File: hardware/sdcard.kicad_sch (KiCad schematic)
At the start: 15 parts, among them J4 MEM2067

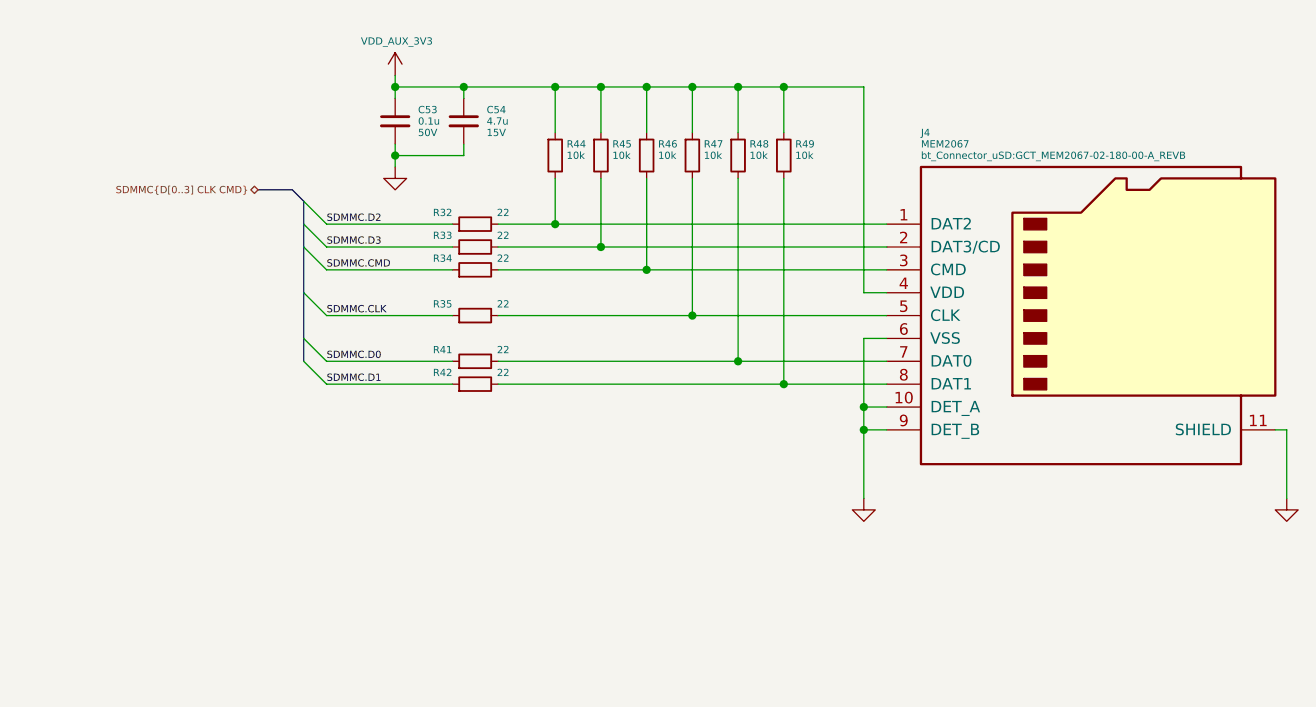
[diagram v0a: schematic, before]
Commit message: minor sch tweaks, more layout, added power emc shield
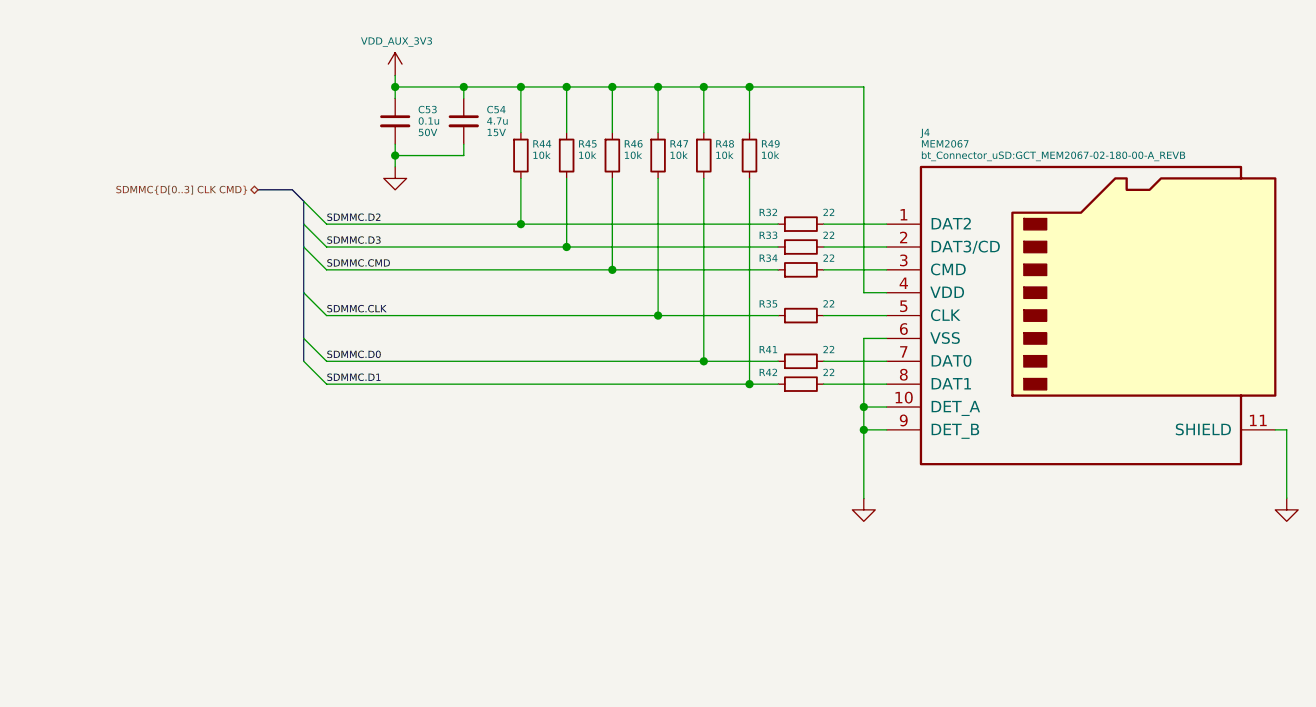
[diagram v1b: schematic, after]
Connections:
- net SDMMC.CLK: now also R47.2
- net SDMMC.CMD: now also R46.2
- net SDMMC.D0: now also R48.2
- net SDMMC.D1: now also R49.2
- net SDMMC.D2: now also R44.2
- net SDMMC.D3: now also R45.2
- net at J4.1 (DAT2), R32.2: no longer R44.2
- net at J4.8 (DAT1), R42.2: no longer R49.2
- net at J4.2 (DAT3/CD), R33.2: no longer R45.2
- net at J4.7 (DAT0), R41.2: no longer R48.2
- net at J4.3 (CMD), R34.2: no longer R46.2
- net at J4.5 (CLK), R35.2: no longer R47.2
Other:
- moved on the sheet: R32, R33, R34, R35, R41, R42, R44, R45, R46, R47, R48, R49

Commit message: Added ESP32-S3-WROOM
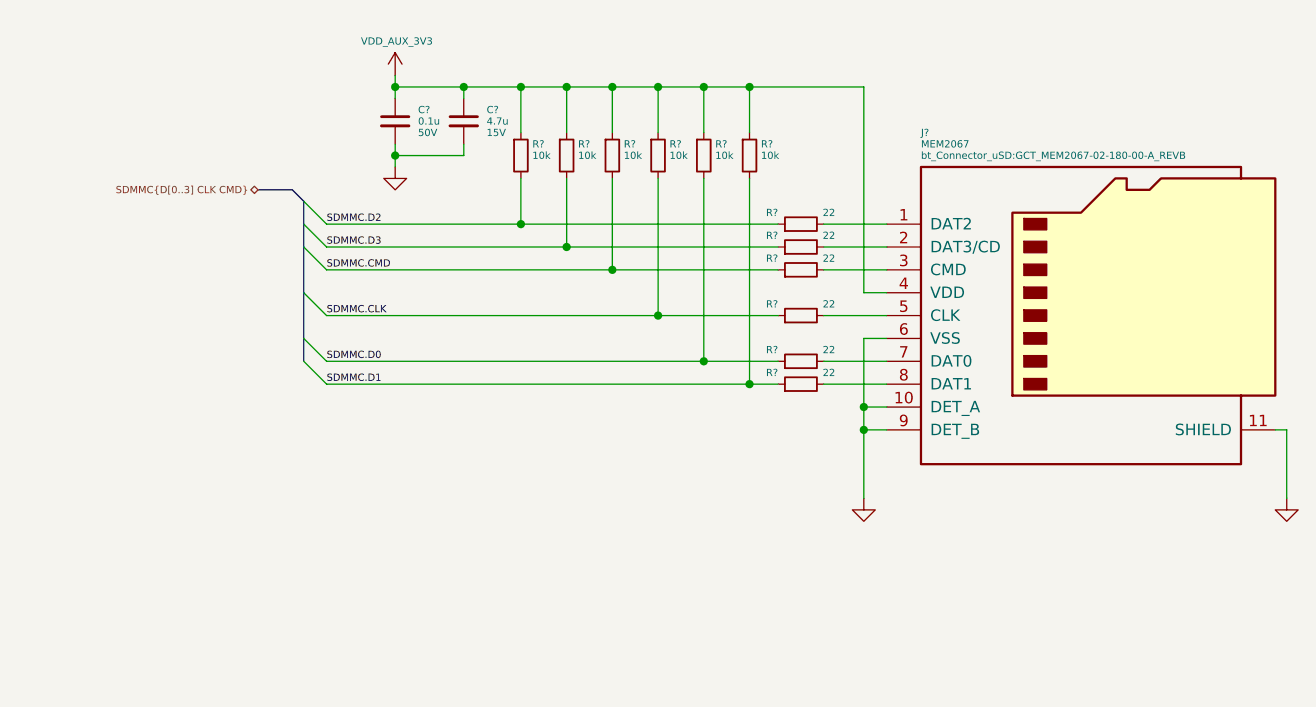
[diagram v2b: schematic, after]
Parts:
- renumbered C54 to C?, C53 to C?, J4 to J?, R44 to R?, R42 to R?, R33 to R?, R49 to R?, R41 to R?, R46 to R?, R45 to R?, R35 to R?, R48 to R?, R32 to R?, R34 to R?, R47 to R?
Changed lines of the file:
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@@
   (symbol (lib_id "Device:R_Small") (at 118.11 82.55 0) (unit 1)
     (in_bom yes) (on_board yes)
-    (property "Reference" "R44" (id 0) (at 119.38 81.28 0)
+    (property "Reference" "R?" (id 0) (at 119.38 81.28 0)
       (effects (font (size 0.8 0.8)) (justify left))
     )
@@
   (symbol (lib_id "Device:R_Small") (at 149.225 107.95 90) (unit 1)
     (in_bom yes) (on_board yes)
-    (property "Reference" "R42" (id 0) (at 146.685 106.68 90)
+    (property "Reference" "R?" (id 0) (at 146.685 106.68 90)
       (effects (font (size 0.8 0.8)) (justify left))
     )
@@
   (symbol (lib_id "Device:C_Small") (at 111.76 78.74 0) (unit 1)
     (in_bom yes) (on_board yes)
-    (property "Reference" "C54" (id 0) (at 114.3 77.47 0)
+    (property "Reference" "C?" (id 0) (at 114.3 77.47 0)
       (effects (font (size 0.8 0.8)) (justify left))
     )
@@
   (symbol (lib_id "bt_power:VDD_AUX_3V3") (at 104.14 73.66 0) (unit 1)
     (in_bom no) (on_board no)
-    (property "Reference" "#U025" (id 0) (at 104.6734 73.66 0)
+    (property "Reference" "#U?" (id 0) (at 104.6734 73.66 0)
       (effects (font (size 1.27 1.27)) hide)
     )
@@
   (symbol (lib_id "Device:R_Small") (at 149.225 92.71 90) (unit 1)
     (in_bom yes) (on_board yes)
-    (property "Reference" "R33" (id 0) (at 146.685 91.44 90)
+    (property "Reference" "R?" (id 0) (at 146.685 91.44 90)
       (effects (font (size 0.8 0.8)) (justify left))
     )
@@
   (symbol (lib_id "Device:R_Small") (at 143.51 82.55 0) (unit 1)
     (in_bom yes) (on_board yes)
-    (property "Reference" "R49" (id 0) (at 144.78 81.28 0)
+    (property "Reference" "R?" (id 0) (at 144.78 81.28 0)
       (effects (font (size 0.8 0.8)) (justify left))
     )
@@
   (symbol (lib_id "Device:R_Small") (at 149.225 105.41 90) (unit 1)
     (in_bom yes) (on_board yes)
-    (property "Reference" "R41" (id 0) (at 146.685 104.14 90)
+    (property "Reference" "R?" (id 0) (at 146.685 104.14 90)
       (effects (font (size 0.8 0.8)) (justify left))
     )
@@
   (symbol (lib_id "power:GND") (at 156.21 120.65 0) (unit 1)
     (in_bom yes) (on_board yes)
-    (property "Reference" "#PWR072" (id 0) (at 156.21 127 0)
+    (property "Reference" "#PWR?" (id 0) (at 156.21 127 0)
       (effects (font (size 0.8 0.8)) hide)
     )
@@
   (symbol (lib_id "Device:R_Small") (at 128.27 82.55 0) (unit 1)
     (in_bom yes) (on_board yes)
-    (property "Reference" "R46" (id 0) (at 129.54 81.28 0)
+    (property "Reference" "R?" (id 0) (at 129.54 81.28 0)
       (effects (font (size 0.8 0.8)) (justify left))
     )
@@
   (symbol (lib_id "Device:R_Small") (at 123.19 82.55 0) (unit 1)
     (in_bom yes) (on_board yes)
-    (property "Reference" "R45" (id 0) (at 124.46 81.28 0)
+    (property "Reference" "R?" (id 0) (at 124.46 81.28 0)
       (effects (font (size 0.8 0.8)) (justify left))
     )
@@
   (symbol (lib_id "power:GND") (at 104.14 83.82 0) (mirror y) (unit 1)
     (in_bom yes) (on_board yes)
-    (property "Reference" "#PWR071" (id 0) (at 104.14 90.17 0)
+    (property "Reference" "#PWR?" (id 0) (at 104.14 90.17 0)
       (effects (font (size 0.8 0.8)) hide)
     )
@@
   (symbol (lib_id "Device:R_Small") (at 149.225 100.33 90) (unit 1)
     (in_bom yes) (on_board yes)
-    (property "Reference" "R35" (id 0) (at 146.685 99.06 90)
+    (property "Reference" "R?" (id 0) (at 146.685 99.06 90)
       (effects (font (size 0.8 0.8)) (justify left))
     )
@@
   (symbol (lib_id "Device:R_Small") (at 138.43 82.55 0) (unit 1)
     (in_bom yes) (on_board yes)
-    (property "Reference" "R48" (id 0) (at 139.7 81.28 0)
+    (property "Reference" "R?" (id 0) (at 139.7 81.28 0)
       (effects (font (size 0.8 0.8)) (justify left))
     )
@@
   (symbol (lib_id "power:GND") (at 203.2 120.65 0) (unit 1)
     (in_bom yes) (on_board yes)
-    (property "Reference" "#PWR073" (id 0) (at 203.2 127 0)
+    (property "Reference" "#PWR?" (id 0) (at 203.2 127 0)
       (effects (font (size 0.8 0.8)) hide)
     )
@@
   (symbol (lib_id "Device:C_Small") (at 104.14 78.74 0) (unit 1)
     (in_bom yes) (on_board yes)
-    (property "Reference" "C53" (id 0) (at 106.68 77.47 0)
+    (property "Reference" "C?" (id 0) (at 106.68 77.47 0)
       (effects (font (size 0.8 0.8)) (justify left))
     )
@@
   (symbol (lib_id "Connector:Micro_SD_Card_Det") (at 181.61 100.33 0) (unit 1)
     (in_bom yes) (on_board yes)
-    (property "Reference" "J4" (id 0) (at 162.56 80.01 0)
+    (property "Reference" "J?" (id 0) (at 162.56 80.01 0)
       (effects (font (size 0.8 0.8)) (justify left))
     )
@@
   (symbol (lib_id "Device:R_Small") (at 149.225 90.17 90) (unit 1)
     (in_bom yes) (on_board yes)
-    (property "Reference" "R32" (id 0) (at 146.685 88.9 90)
+    (property "Reference" "R?" (id 0) (at 146.685 88.9 90)
       (effects (font (size 0.8 0.8)) (justify left))
     )
@@
   (symbol (lib_id "Device:R_Small") (at 149.225 95.25 90) (unit 1)
     (in_bom yes) (on_board yes)
-    (property "Reference" "R34" (id 0) (at 146.685 93.98 90)
+    (property "Reference" "R?" (id 0) (at 146.685 93.98 90)
       (effects (font (size 0.8 0.8)) (justify left))
     )
@@
   (symbol (lib_id "Device:R_Small") (at 133.35 82.55 0) (unit 1)
     (in_bom yes) (on_board yes)
-    (property "Reference" "R47" (id 0) (at 134.62 81.28 0)
-      (effects (font (size 0.8 0.8)) (justify left))
-    )
+    (property "Reference" "R?" (id 0) (at 134.62 81.28 0)
+      (effects (font (size 0.8 0.8)) (justify left))
+    )

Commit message: changing sdmmc to spi to support lcd rgb mode
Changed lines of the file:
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@@
   (junction (at 128.27 74.93) (diameter 0) (color 0 0 0 0)
   )
+  (bus_entry (at 90.17 135.89) (size 2.54 -2.54)
+    (stroke (width 0) (type default) (color 0 0 0 0))
+  )
+  (bus_entry (at 92.71 125.73) (size -2.54 2.54)
+    (stroke (width 0) (type default) (color 0 0 0 0))
+  )
+  (bus_entry (at 92.71 130.81) (size -2.54 2.54)
+    (stroke (width 0) (type default) (color 0 0 0 0))
+  )
   (bus_entry (at 93.98 92.71) (size 2.54 2.54)
     (stroke (width 0) (type default) (color 0 0 0 0))
@@
     (stroke (width 0) (type default) (color 0 0 0 0))
   )
+  (bus_entry (at 92.71 133.35) (size -2.54 2.54)
+    (stroke (width 0) (type default) (color 0 0 0 0))
+  )
   (bus_entry (at 93.98 97.79) (size 2.54 2.54)
     (stroke (width 0) (type default) (color 0 0 0 0))
@@
     (stroke (width 0) (type default) (color 0 0 0 0))
   )
+  (bus_entry (at 92.71 130.81) (size -2.54 2.54)
+    (stroke (width 0) (type default) (color 0 0 0 0))
+  )
   (wire (pts (xy 123.19 74.93) (xy 128.27 74.93))
     (stroke (width 0) (type default) (color 0 0 0 0))
@@
     (stroke (width 0) (type default) (color 0 0 0 0))
   )
+  (wire (pts (xy 62.23 133.35) (xy 90.17 133.35))
+    (stroke (width 0) (type default) (color 0 0 0 0))
+  )
+  (bus (pts (xy 92.71 130.81) (xy 92.71 133.35))
+    (stroke (width 0) (type default) (color 0 0 0 0))
+  )
   (wire (pts (xy 123.19 85.09) (xy 123.19 92.71))
     (stroke (width 0) (type default) (color 0 0 0 0))
@@
     (stroke (width 0) (type default) (color 0 0 0 0))
   )
+  (bus (pts (xy 93.98 124.46) (xy 96.52 124.46))
+    (stroke (width 0) (type default) (color 0 0 0 0))
+  )
+  (wire (pts (xy 62.23 135.89) (xy 90.17 135.89))
+    (stroke (width 0) (type default) (color 0 0 0 0))
+  )
   (wire (pts (xy 128.27 95.25) (xy 146.685 95.25))
     (stroke (width 0) (type default) (color 0 0 0 0))
@@
     (stroke (width 0) (type default) (color 0 0 0 0))
   )
+  (bus (pts (xy 92.71 125.73) (xy 93.98 124.46))
+    (stroke (width 0) (type default) (color 0 0 0 0))
+  )
   (wire (pts (xy 151.765 105.41) (xy 158.75 105.41))
     (stroke (width 0) (type default) (color 0 0 0 0))
@@
     (stroke (width 0) (type default) (color 0 0 0 0))
   )
+  (bus (pts (xy 92.71 125.73) (xy 92.71 130.81))
+    (stroke (width 0) (type default) (color 0 0 0 0))
+  )
   (wire (pts (xy 156.21 97.79) (xy 158.75 97.79))
     (stroke (width 0) (type default) (color 0 0 0 0))
@@
     (stroke (width 0) (type default) (color 0 0 0 0))
   )
+  (wire (pts (xy 62.23 128.27) (xy 90.17 128.27))
+    (stroke (width 0) (type default) (color 0 0 0 0))
+  )
   (bus (pts (xy 93.98 92.71) (xy 93.98 97.79))
     (stroke (width 0) (type default) (color 0 0 0 0))
@@
     (stroke (width 0) (type default) (color 0 0 0 0))
   )
+  (wire (pts (xy 62.23 140.97) (xy 80.01 140.97))
+    (stroke (width 0) (type default) (color 0 0 0 0))
+  )
   (wire (pts (xy 118.11 85.09) (xy 118.11 90.17))
     (stroke (width 0) (type default) (color 0 0 0 0))
@@
     (effects (font (size 0.8 0.8)) (justify left bottom))
   )
+  (label "SPI_SD_LCD.MISO" (at 90.17 133.35 180)
+    (effects (font (size 0.8 0.8)) (justify right bottom))
+  )
   (label "SDMMC.CLK" (at 96.52 100.33 0)
     (effects (font (size 0.8 0.8)) (justify left bottom))
@@
     (effects (font (size 0.8 0.8)) (justify left bottom))
   )
+  (label "SPI_SD_LCD.MOSI" (at 90.17 135.89 180)
+    (effects (font (size 0.8 0.8)) (justify right bottom))
+  )
   (label "SDMMC.D0" (at 96.52 105.41 0)
     (effects (font (size 0.8 0.8)) (justify left bottom))
+  )
+  (label "SPI_SD_LCD.SCLK" (at 90.17 128.27 180)
+    (effects (font (size 0.8 0.8)) (justify right bottom))
   )
   (hierarchical_label "SDMMC{D[0..3] CLK CMD}" (shape bidirectional) (at 88.9 86.36 180)
     (effects (font (size 0.8 0.8)) (justify right))
   )
+  (hierarchical_label "SPI_SD_CS" (shape input) (at 80.01 140.97 0)
+    (effects (font (size 0.8 0.8)) (justify left))
+  )
+  (hierarchical_label "SPI_SD_LCD{MISO MOSI SCLK}" (shape bidirectional) (at 96.52 124.46 0)
+    (effects (font (size 0.8 0.8)) (justify left))
+  )
   (symbol (lib_id "Device:R_Small") (at 118.11 82.55 0) (unit 1)

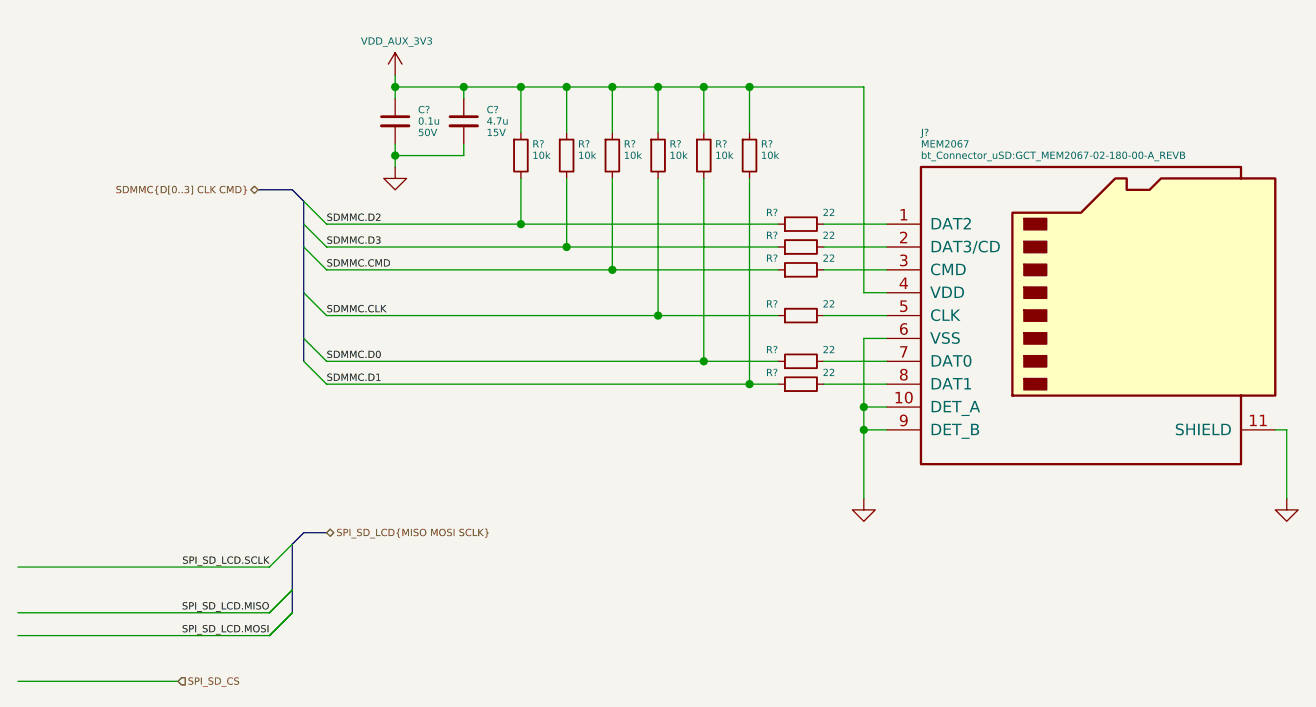
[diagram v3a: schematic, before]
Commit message: layout 0 unconnected
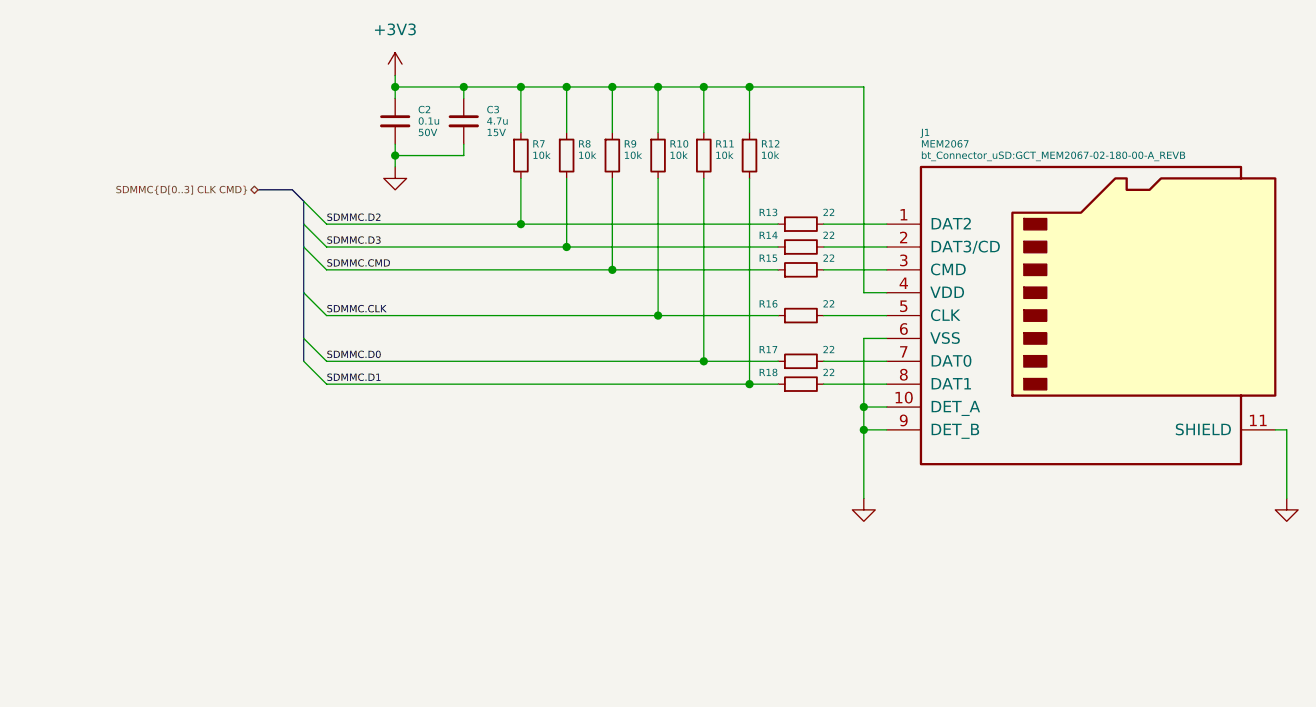
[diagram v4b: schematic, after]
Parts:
- gave numbers to parts that had none: 15
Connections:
- net VDD_AUX_3V3 renamed +3V3
